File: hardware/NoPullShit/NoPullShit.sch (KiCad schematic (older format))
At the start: 47 parts, among them J1 USB Power, J2 Load cell, J3 Batt+, J4 Batt-, J5 ICSP, J6 UART, J7 Spk+, J8 Spk-, Q1 S8550, Q2 S8050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

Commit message: Footprint assignment + initial grouping
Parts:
- removed Q1, Q3: S8550, Package_TO_SOT_THT:TO-92_Inline, symbol Transistor_BJT:S8550
- removed Q2: S8050, Package_TO_SOT_THT:TO-92_Inline, symbol Transistor_BJT:S8050
- added C14: 100u, Capacitor_SMD:C_1206_3216Metric, symbol Device:C
- added Q1, Q3: BC808, Package_TO_SOT_SMD:SOT-23, symbol Transistor_BJT:BC808
- added Q2: BC817, Package_TO_SOT_SMD:SOT-23, symbol Transistor_BJT:BC817
- added R5: 1R, Resistor_SMD:R_0603_1608Metric, symbol Device:R
- C1, C10, C11, C12, C2, C3, C4, C5, C6, C7, C8, C9: footprint (none) -> Capacitor_SMD:C_0603_1608Metric
- C13: value 220u -> 100u; footprint (none) -> Capacitor_SMD:C_1206_3216Metric
- D1: footprint (none) -> LED_SMD:LED_0603_1608Metric
- J1: footprint (none) -> Libraries:AMPHENOL_10118194-0001LF
- J2, J6: footprint (none) -> Connector_PinHeader_2.54mm:PinHeader_1x04_P2.54mm_Vertical
- J3, J4, J7, J8: footprint (none) -> Connector_PinHeader_1.00mm:PinHeader_1x01_P1.00mm_Vertical
- J5: footprint (none) -> Connector_PinHeader_2.54mm:PinHeader_2x03_P2.54mm_Vertical
- PTC1, R1, R2, R3: footprint (none) -> Resistor_SMD:R_0603_1608Metric
- R10: renamed from R9; footprint (none) -> Resistor_SMD:R_0603_1608Metric
- R11: renamed from R10; footprint (none) -> Resistor_SMD:R_0603_1608Metric
- R12: renamed from R11; footprint (none) -> Resistor_SMD:R_0603_1608Metric
- R13: renamed from R12; footprint (none) -> Resistor_SMD:R_0603_1608Metric
- R14: renamed from R13; footprint (none) -> Resistor_SMD:R_0603_1608Metric
- R15: renamed from R14; footprint (none) -> Resistor_SMD:R_0603_1608Metric
- R16: renamed from R15; footprint (none) -> Resistor_SMD:R_0603_1608Metric
- R17: renamed from R16; footprint (none) -> Resistor_SMD:R_0603_1608Metric
- R18: renamed from R17; footprint (none) -> Resistor_SMD:R_0603_1608Metric
- R4: value 0R4 1/4W -> 1R; footprint (none) -> Resistor_SMD:R_0603_1608Metric
- R6: renamed from R5; footprint (none) -> Resistor_SMD:R_0603_1608Metric
- R7: renamed from R6; footprint (none) -> Resistor_SMD:R_0603_1608Metric
- R8: renamed from R7; footprint (none) -> Resistor_SMD:R_0603_1608Metric
- R9: renamed from R8; footprint (none) -> Resistor_SMD:R_0603_1608Metric
- U1: footprint (none) -> Package_SO:SOP-16_3.9x9.9mm_P1.27mm
- U2: footprint (none) -> Package_SO:SOP-8_3.9x4.9mm_P1.27mm
- Y1: footprint (none) -> Crystal:Crystal_SMD_ECS_CSM3X-2Pin_7.6x4.1mm
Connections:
- net GND: now also Q3.3 (C)
- net VCC: now also Q2.3 (C)
- net at C5.2, R8.1, U1.1 (Vsup)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: now also Q1.2 (E)
- net at U1.2 (Base): now also Q1.1 (B)
- net at C1.1, J2.1 (Pin_1), R7.1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: now also Q1.3 (C)
- net at C13.2: now also C14.2, Q2.2 (E), Q3.2 (E)
- net at R18.1: now also Q2.1 (B), Q3.1 (B)
- net at C3.1, R10.1, R4.1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: now also R5.1
- net at J1.1 (VBUS), R4.2: now also R5.2
- net at C13.1, J7.1 (Pin_1): now also C14.1
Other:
- moved on the sheet: C13, J8

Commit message: Initial routing backup
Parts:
- added H1, H2, H3, H4: MountingHole_Pad, MountingHole:MountingHole_2.2mm_M2_Pad_Via, symbol Mechanical:MountingHole_Pad
- J2: footprint Connector_PinHeader_2.54mm:PinHeader_1x04_P2.54mm_Vertical -> Connector_PinHeader_2.00mm:PinHeader_1x04_P2.00mm_Vertical
- J3, J4, J7, J8: footprint Connector_PinHeader_1.00mm:PinHeader_1x01_P1.00mm_Vertical -> TestPoint:TestPoint_THTPad_1.0x1.0mm_Drill0.5mm
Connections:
- net GND: now also H1.1, H2.1, H3.1, H4.1
- net LED_A: now also U3.10 (PD6); no longer U3.2 (PD4)
- net N_BATT_CHRG: now also U3.26 (PC3); no longer U3.10 (PD6)
- net N_BATT_STDBY: now also U3.25 (PC2); no longer U3.11 (PD7)
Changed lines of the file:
@@
 F 0 "J2" H 850 4700 50  0000 C CNN
 F 1 "Load cell" V 950 4450 50  0000 C CNN
-F 2 "Connector_PinHeader_2.54mm:PinHeader_1x04_P2.54mm_Vertical" H 850 4500 50  0001 C CNN
+F 2 "Connector_PinHeader_2.00mm:PinHeader_1x04_P2.00mm_Vertical" H 850 4500 50  0001 C CNN
 F 3 "~" H 850 4500 50  0001 C CNN
 	1    850  4500
@@
 Wire Wire Line
 	6800 4400 8500 4400
-Text Label 6800 4700 0    50   ~ 0
+Text Label 6800 4900 0    50   ~ 0
 LED_A
 Text Label 7400 1100 2    50   ~ 0
@@
 	6800 3500 8600 3500
 Connection ~ 8600 3500
-Text Label 6800 5000 0    50   ~ 0
+Text Label 6800 3700 0    50   ~ 0
 N_BATT_STDBY
-Text Label 6800 4900 0    50   ~ 0
+Text Label 6800 3800 0    50   ~ 0
 N_BATT_CHRG
 Wire Wire Line
@@
 F 0 "J7" H 10680 2942 50  0000 L CNN
 F 1 "Spk+" H 10680 2851 50  0000 L CNN
-F 2 "Connector_PinHeader_1.00mm:PinHeader_1x01_P1.00mm_Vertical" H 10600 2900 50  0001 C CNN
+F 2 "TestPoint:TestPoint_THTPad_1.0x1.0mm_Drill0.5mm" H 10600 2900 50  0001 C CNN
 F 3 "~" H 10600 2900 50  0001 C CNN
 	1    10600 2900
@@
 F 0 "J8" H 10680 3192 50  0000 L CNN
 F 1 "Spk-" H 10680 3101 50  0000 L CNN
-F 2 "Connector_PinHeader_1.00mm:PinHeader_1x01_P1.00mm_Vertical" H 10600 3150 50  0001 C CNN
+F 2 "TestPoint:TestPoint_THTPad_1.0x1.0mm_Drill0.5mm" H 10600 3150 50  0001 C CNN
 F 3 "~" H 10600 3150 50  0001 C CNN
 	1    10600 3150
@@
 F 0 "J3" H 5980 792 50  0000 L CNN
 F 1 "Batt+" H 5980 701 50  0000 L CNN
-F 2 "Connector_PinHeader_1.00mm:PinHeader_1x01_P1.00mm_Vertical" H 5900 750 50  0001 C CNN
+F 2 "TestPoint:TestPoint_THTPad_1.0x1.0mm_Drill0.5mm" H 5900 750 50  0001 C CNN
 F 3 "~" H 5900 750 50  0001 C CNN
 	1    5900 750
@@
 F 0 "J4" H 5980 992 50  0000 L CNN
 F 1 "Batt-" H 5980 901 50  0000 L CNN
-F 2 "Connector_PinHeader_1.00mm:PinHeader_1x01_P1.00mm_Vertical" H 5900 950 50  0001 C CNN
+F 2 "TestPoint:TestPoint_THTPad_1.0x1.0mm_Drill0.5mm" H 5900 950 50  0001 C CNN
 F 3 "~" H 5900 950 50  0001 C CNN
 	1    5900 950
@@
 $EndComp
 Connection ~ 9750 2900
+$Comp
+L Mechanical:MountingHole_Pad H1
+U 1 1 60D37706
+P 4750 6950
+F 0 "H1" H 4850 6953 50  0000 L CNN
+F 1 "MountingHole_Pad" H 4850 6908 50  0001 L CNN
+F 2 "MountingHole:MountingHole_2.2mm_M2_Pad_Via" H 4750 6950 50  0001 C CNN
+F 3 "~" H 4750 6950 50  0001 C CNN
+	1    4750 6950
+	1    0    0    -1
+$EndComp
+$Comp
+L Mechanical:MountingHole_Pad H2
+U 1 1 60D3A9F3
+P 5100 6950
+F 0 "H2" H 5200 6953 50  0000 L CNN
+F 1 "MountingHole_Pad" H 5200 6908 50  0001 L CNN
+F 2 "MountingHole:MountingHole_2.2mm_M2_Pad_Via" H 5100 6950 50  0001 C CNN
+F 3 "~" H 5100 6950 50  0001 C CNN
+	1    5100 6950
+	1    0    0    -1
+$EndComp
+$Comp
+L Mechanical:MountingHole_Pad H3
+U 1 1 60D3B2D9
+P 5400 6950
+F 0 "H3" H 5500 6953 50  0000 L CNN
+F 1 "MountingHole_Pad" H 5500 6908 50  0001 L CNN
+F 2 "MountingHole:MountingHole_2.2mm_M2_Pad_Via" H 5400 6950 50  0001 C CNN
+F 3 "~" H 5400 6950 50  0001 C CNN
+	1    5400 6950
+	1    0    0    -1
+$EndComp
+$Comp
+L Mechanical:MountingHole_Pad H4
+U 1 1 60D3B796
+P 5700 6950
+F 0 "H4" H 5800 6953 50  0000 L CNN
+F 1 "MountingHole_Pad" H 5800 6908 50  0001 L CNN
+F 2 "MountingHole:MountingHole_2.2mm_M2_Pad_Via" H 5700 6950 50  0001 C CNN
+F 3 "~" H 5700 6950 50  0001 C CNN
+	1    5700 6950
+	1    0    0    -1
+$EndComp
+$Comp
+L power:GND #PWR0101
+U 1 1 60D3D771
+P 5250 7050
+F 0 "#PWR0101" H 5250 6800 50  0001 C CNN
+F 1 "GND" H 5255 6877 50  0000 C CNN
+F 2 "" H 5250 7050 50  0001 C CNN
+F 3 "" H 5250 7050 50  0001 C CNN
+	1    5250 7050
+	1    0    0    -1
+$EndComp
+Wire Wire Line
+	4750 7050 5100 7050
+Connection ~ 5100 7050
+Wire Wire Line
+	5100 7050 5250 7050
+Connection ~ 5250 7050
+Wire Wire Line
+	5250 7050 5400 7050
+Connection ~ 5400 7050
+Wire Wire Line
+	5400 7050 5700 7050
 $EndSCHEMATC

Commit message: Finished initla routing
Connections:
- net DOUT: now also U3.1 (PD3); no longer U3.32 (PD2)
- net RATE: now also U3.32 (PD2); no longer U3.1 (PD3)
- net SCK: now also U3.2 (PD4); no longer U3.14 (PB2)
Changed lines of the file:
@@
 Text Label 4050 5000 0    50   ~ 0
-RATE
-Text Label 6800 2800 0    50   ~ 0
-SCK
-Text Label 6800 4500 0    50   ~ 0
-DOUT
-Text Label 6800 4600 0    50   ~ 0
 RATE
 $Comp
@@
 Wire Wire Line
 	5400 7050 5700 7050
+Text Label 6800 4700 0    50   ~ 0
+SCK
+Text Label 6800 4600 0    50   ~ 0
+DOUT
+Text Label 6800 4500 0    50   ~ 0
+RATE
 $EndSCHEMATC

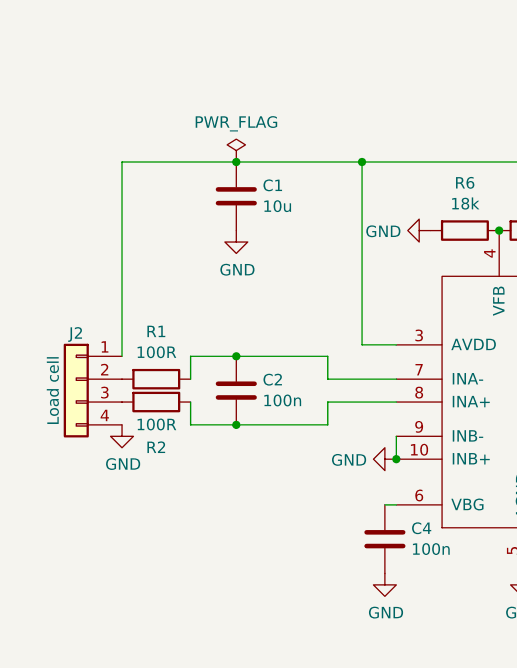
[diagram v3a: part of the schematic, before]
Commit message: Small layout changes
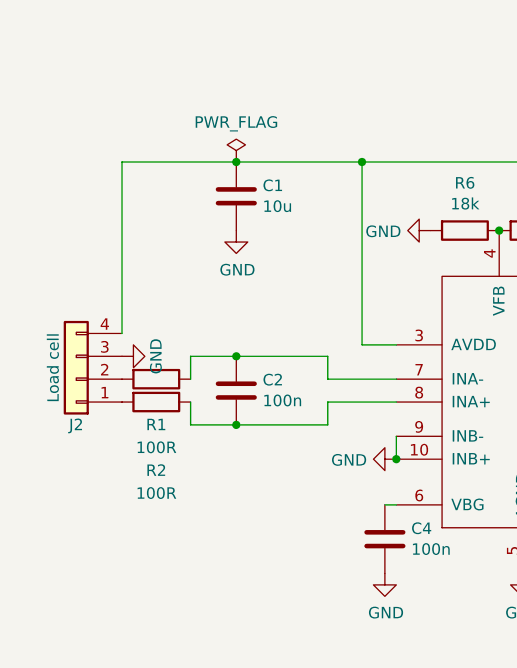
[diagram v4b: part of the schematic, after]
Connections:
- net GND: now also J2.3 (Pin_3); no longer J2.4 (Pin_4)
- net at C1.1, Q1.3 (C), R7.1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: now also J2.4 (Pin_4); no longer J2.1 (Pin_1)
- net at R2.2: now also J2.1 (Pin_1); no longer J2.3 (Pin_3)
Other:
- moved on the sheet: J2
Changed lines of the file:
@@
 U 1 1 60CD8B1B
 P 1200 4600
-F 0 "R2" V 1400 4600 50  0000 C CNN
-F 1 "100R" V 1300 4600 50  0000 C CNN
+F 0 "R2" V 1500 4600 50  0000 C CNN
+F 1 "100R" V 1600 4600 50  0000 C CNN
 F 2 "Resistor_SMD:R_0603_1608Metric" V 1130 4600 50  0001 C CNN
 F 3 "~" H 1200 4600 50  0001 C CNN
@@
 U 1 1 60CD638C
 P 1200 4500
-F 0 "R1" V 993 4500 50  0000 C CNN
-F 1 "100R" V 1084 4500 50  0000 C CNN
+F 0 "R1" V 1400 4500 50  0000 C CNN
+F 1 "100R" V 1500 4500 50  0000 C CNN
 F 2 "Resistor_SMD:R_0603_1608Metric" V 1130 4500 50  0001 C CNN
 F 3 "~" H 1200 4500 50  0001 C CNN
@@
 F 3 "~" H 850 4500 50  0001 C CNN
 	1    850  4500
-	-1   0    0    -1
+	-1   0    0    1
 $EndComp
 $Comp
 L power:GND #PWR03
 U 1 1 60D4BE2C
-P 1050 4700
-F 0 "#PWR03" H 1050 4450 50  0001 C CNN
-F 1 "GND" H 1055 4527 50  0000 C CNN
-F 2 "" H 1050 4700 50  0001 C CNN
-F 3 "" H 1050 4700 50  0001 C CNN
-	1    1050 4700
-	1    0    0    -1
-$EndComp
-Wire Wire Line
-	1050 4400 1050 3550
+P 1050 4400
+F 0 "#PWR03" H 1050 4150 50  0001 C CNN
+F 1 "GND" H 1050 4250 50  0000 C CNN
+F 2 "" H 1050 4400 50  0001 C CNN
+F 3 "" H 1050 4400 50  0001 C CNN
+	1    1050 4400
+	0    -1   -1   0
+$EndComp
 Wire Wire Line
 	2100 3550 3000 3550
@@
 Text Label 6800 4500 0    50   ~ 0
 RATE
+Wire Wire Line
+	1050 3550 1050 4300
 $EndSCHEMATC

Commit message: Small small changes
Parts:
- C1, C3, C6: footprint Capacitor_SMD:C_0603_1608Metric -> Capacitor_SMD:C_0805_2012Metric
- J1: footprint Libraries:AMPHENOL_10118194-0001LF -> Connector_USB:USB_Micro-B_Amphenol_10103594-0001LF_Horizontal
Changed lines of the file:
@@
 F 0 "J1" H 857 1667 50  0000 C CNN
 F 1 "USB Power" H 857 1576 50  0000 C CNN
-F 2 "Libraries:AMPHENOL_10118194-0001LF" H 950 1150 50  0001 C CNN
+F 2 "Connector_USB:USB_Micro-B_Amphenol_10103594-0001LF_Horizontal" H 950 1150 50  0001 C CNN
 F 3 "~" H 950 1150 50  0001 C CNN
 	1    800  1200
@@
 F 0 "C3" H 2315 1196 50  0000 L CNN
 F 1 "10u" H 2315 1105 50  0000 L CNN
-F 2 "Capacitor_SMD:C_0603_1608Metric" H 2238 1000 50  0001 C CNN
+F 2 "Capacitor_SMD:C_0805_2012Metric" H 2238 1000 50  0001 C CNN
 F 3 "~" H 2200 1150 50  0001 C CNN
 	1    2200 1150
@@
 F 0 "C6" H 5465 1296 50  0000 L CNN
 F 1 "10u" H 5465 1205 50  0000 L CNN
-F 2 "Capacitor_SMD:C_0603_1608Metric" H 5388 1100 50  0001 C CNN
+F 2 "Capacitor_SMD:C_0805_2012Metric" H 5388 1100 50  0001 C CNN
 F 3 "~" H 5350 1250 50  0001 C CNN
 	1    5350 1250
@@
 F 0 "C1" H 1665 3746 50  0000 L CNN
 F 1 "10u" H 1665 3655 50  0000 L CNN
-F 2 "Capacitor_SMD:C_0603_1608Metric" H 1588 3550 50  0001 C CNN
+F 2 "Capacitor_SMD:C_0805_2012Metric" H 1588 3550 50  0001 C CNN
 F 3 "~" H 1550 3700 50  0001 C CNN
 	1    1550 3700

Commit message: More smaller, more better
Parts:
- removed R13: 0R, Resistor_SMD:R_0603_1608Metric, symbol Device:R
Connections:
- net VCC: now also C8.1, C9.2, U3.18 (AVCC), U3.4 (VCC), U3.6 (VCC)
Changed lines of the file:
@@
-	1    0    0    -1
-$EndComp
-$Comp
-L power:VCC #PWR022
-U 1 1 60C15EE1
-P 6200 1550
-F 0 "#PWR022" H 6200 1400 50  0001 C CNN
-F 1 "VCC" H 6217 1723 50  0000 C CNN
-F 2 "" H 6200 1550 50  0001 C CNN
-F 3 "" H 6200 1550 50  0001 C CNN
-	1    6200 1550
 	1    0    0    -1
 $EndComp
@@
 Wire Wire Line
 	6300 1850 6300 2200
-Connection ~ 6200 1850
 Connection ~ 6300 2200
 $Comp
@@
 $EndComp
 $Comp
-L Device:R R13
-U 1 1 60D63711
-P 6200 1700
-F 0 "R13" H 6130 1654 50  0000 R CNN
-F 1 "0R" H 6130 1745 50  0000 R CNN
-F 2 "Resistor_SMD:R_0603_1608Metric" V 6130 1700 50  0001 C CNN
-F 3 "~" H 6200 1700 50  0001 C CNN
-	1    6200 1700
-	-1   0    0    1
-$EndComp
-$Comp
 L Connector_Generic:Conn_01x04 J6
 U 1 1 60D6D08D
@@
 	1    0    0    -1
 $EndComp
-$Comp
-L power:PWR_FLAG #FLG05
-U 1 1 60BED3FB
-P 6550 1550
-F 0 "#FLG05" H 6550 1625 50  0001 C CNN
-F 1 "PWR_FLAG" H 6550 1723 50  0000 C CNN
-F 2 "" H 6550 1550 50  0001 C CNN
-F 3 "~" H 6550 1550 50  0001 C CNN
-	1    6550 1550
-	1    0    0    -1
-$EndComp
-Wire Wire Line
-	6550 1550 6550 1850
-Wire Wire Line
-	6550 1850 6300 1850
-Connection ~ 6300 1850
 Wire Wire Line
 	5350 750  5700 750
@@
 Wire Wire Line
 	1050 3550 1050 4300
+$Comp
+L power:VCC #PWR022
+U 1 1 60C15EE1
+P 6200 1850
+F 0 "#PWR022" H 6200 1700 50  0001 C CNN
+F 1 "VCC" H 6217 2023 50  0000 C CNN
+F 2 "" H 6200 1850 50  0001 C CNN
+F 3 "" H 6200 1850 50  0001 C CNN
+	1    6200 1850
+	1    0    0    -1
+$EndComp
+Connection ~ 6200 1850
 $EndSCHEMATC

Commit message: Neatify
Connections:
- net N_BATT_CHRG: now also U3.25 (PC2); no longer U3.26 (PC3)
- net N_BATT_STDBY: now also U3.26 (PC3); no longer U3.25 (PC2)
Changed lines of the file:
@@
 	6800 3500 8600 3500
 Connection ~ 8600 3500
+Text Label 6800 3800 0    50   ~ 0
+N_BATT_STDBY
 Text Label 6800 3700 0    50   ~ 0
-N_BATT_STDBY
-Text Label 6800 3800 0    50   ~ 0
 N_BATT_CHRG
 Wire Wire Line

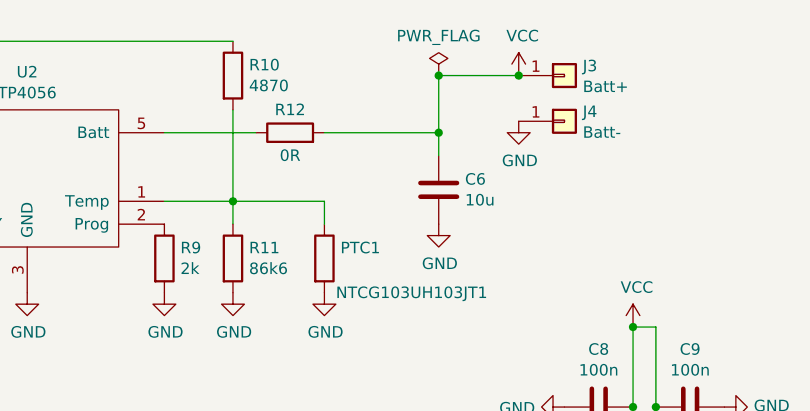
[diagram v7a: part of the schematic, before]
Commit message: PSU current sense fix + some shuffling
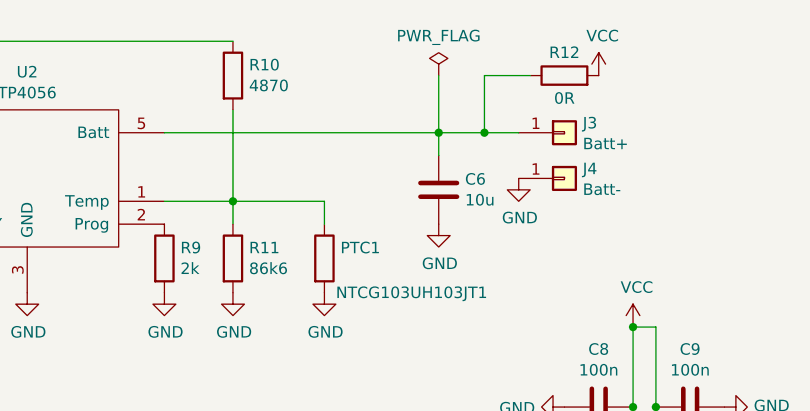
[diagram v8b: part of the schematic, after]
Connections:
- net VCC: no longer C6.1, J3.1 (Pin_1)
- net at R12.1, U2.5 (Batt): now also C6.1, J3.1 (Pin_1)
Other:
- moved on the sheet: J3, J4, R12
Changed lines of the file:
@@
 L power:GND #PWR020
 U 1 1 60C09EC3
-P 5700 950
-F 0 "#PWR020" H 5700 700 50  0001 C CNN
-F 1 "GND" H 5705 777 50  0000 C CNN
-F 2 "" H 5700 950 50  0001 C CNN
-F 3 "" H 5700 950 50  0001 C CNN
-	1    5700 950
+P 5700 1200
+F 0 "#PWR020" H 5700 950 50  0001 C CNN
+F 1 "GND" H 5705 1027 50  0000 C CNN
+F 2 "" H 5700 1200 50  0001 C CNN
+F 3 "" H 5700 1200 50  0001 C CNN
+	1    5700 1200
 	1    0    0    -1
 $EndComp
@@
 L power:VCC #PWR019
 U 1 1 60C14756
-P 5700 750
-F 0 "#PWR019" H 5700 600 50  0001 C CNN
-F 1 "VCC" H 5717 923 50  0000 C CNN
-F 2 "" H 5700 750 50  0001 C CNN
-F 3 "" H 5700 750 50  0001 C CNN
-	1    5700 750
+P 6050 750
+F 0 "#PWR019" H 6050 600 50  0001 C CNN
+F 1 "VCC" H 6067 923 50  0000 C CNN
+F 2 "" H 6050 750 50  0001 C CNN
+F 3 "" H 6050 750 50  0001 C CNN
+	1    6050 750
 	1    0    0    -1
 $EndComp
@@
 L Device:R R12
 U 1 1 60DC0B90
-P 4700 1000
-F 0 "R12" V 4800 1000 50  0000 C CNN
-F 1 "0R" V 4600 1000 50  0000 C CNN
-F 2 "Resistor_SMD:R_0603_1608Metric" V 4630 1000 50  0001 C CNN
-F 3 "~" H 4700 1000 50  0001 C CNN
-	1    4700 1000
+P 5900 750
+F 0 "R12" V 6000 750 50  0000 C CNN
+F 1 "0R" V 5800 750 50  0000 C CNN
+F 2 "Resistor_SMD:R_0603_1608Metric" V 5830 750 50  0001 C CNN
+F 3 "~" H 5900 750 50  0001 C CNN
+	1    5900 750
 	0    -1   -1   0
 $EndComp
-Wire Wire Line
-	4550 1000 4150 1000
 Connection ~ 5350 1000
 Text Label 4050 4500 0    50   ~ 0
@@
 Wire Wire Line
 	4450 1300 4850 1300
-Wire Wire Line
-	4850 1000 5350 1000
 $Comp
 L Connector_Generic:Conn_01x01 J7
@@
 $EndComp
 $Comp
-L Connector_Generic:Conn_01x01 J3
-U 1 1 60F3305D
-P 5900 750
-F 0 "J3" H 5980 792 50  0000 L CNN
-F 1 "Batt+" H 5980 701 50  0000 L CNN
-F 2 "TestPoint:TestPoint_THTPad_1.0x1.0mm_Drill0.5mm" H 5900 750 50  0001 C CNN
-F 3 "~" H 5900 750 50  0001 C CNN
-	1    5900 750
-	1    0    0    -1
-$EndComp
-$Comp
 L Connector_Generic:Conn_01x01 J4
 U 1 1 60F3415B
-P 5900 950
-F 0 "J4" H 5980 992 50  0000 L CNN
-F 1 "Batt-" H 5980 901 50  0000 L CNN
-F 2 "TestPoint:TestPoint_THTPad_1.0x1.0mm_Drill0.5mm" H 5900 950 50  0001 C CNN
-F 3 "~" H 5900 950 50  0001 C CNN
-	1    5900 950
+P 5900 1200
+F 0 "J4" H 5980 1242 50  0000 L CNN
+F 1 "Batt-" H 5980 1151 50  0000 L CNN
+F 2 "TestPoint:TestPoint_THTPad_1.0x1.0mm_Drill0.5mm" H 5900 1200 50  0001 C CNN
+F 3 "~" H 5900 1200 50  0001 C CNN
+	1    5900 1200
 	1    0    0    -1
 $EndComp
 Wire Wire Line
 	5350 750  5350 1000
-Connection ~ 5700 750
 $Comp
 L Device:R R3
@@
 $EndComp
 Wire Wire Line
-	5350 750  5700 750
+	5350 1000 5550 1000
 $Comp
 L power:PWR_FLAG #FLG04
@@
 	1    0    0    -1
 $EndComp
-Connection ~ 5350 750
 $Comp
 L power:PWR_FLAG #FLG02
@@
 $EndComp
 Connection ~ 6200 1850
+Wire Wire Line
+	4150 1000 5350 1000
+$Comp
+L Connector_Generic:Conn_01x01 J3
+U 1 1 60F3305D
+P 5900 1000
+F 0 "J3" H 5980 1042 50  0000 L CNN
+F 1 "Batt+" H 5980 951 50  0000 L CNN
+F 2 "TestPoint:TestPoint_THTPad_1.0x1.0mm_Drill0.5mm" H 5900 1000 50  0001 C CNN
+F 3 "~" H 5900 1000 50  0001 C CNN
+	1    5900 1000
+	1    0    0    -1
+$EndComp
+Wire Wire Line
+	5750 750  5550 750
+Wire Wire Line
+	5550 750  5550 1000
+Connection ~ 5550 1000
+Wire Wire Line
+	5550 1000 5700 1000
 $EndSCHEMATC
